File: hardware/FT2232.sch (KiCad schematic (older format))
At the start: 3 parts, among them U1 FT2232D

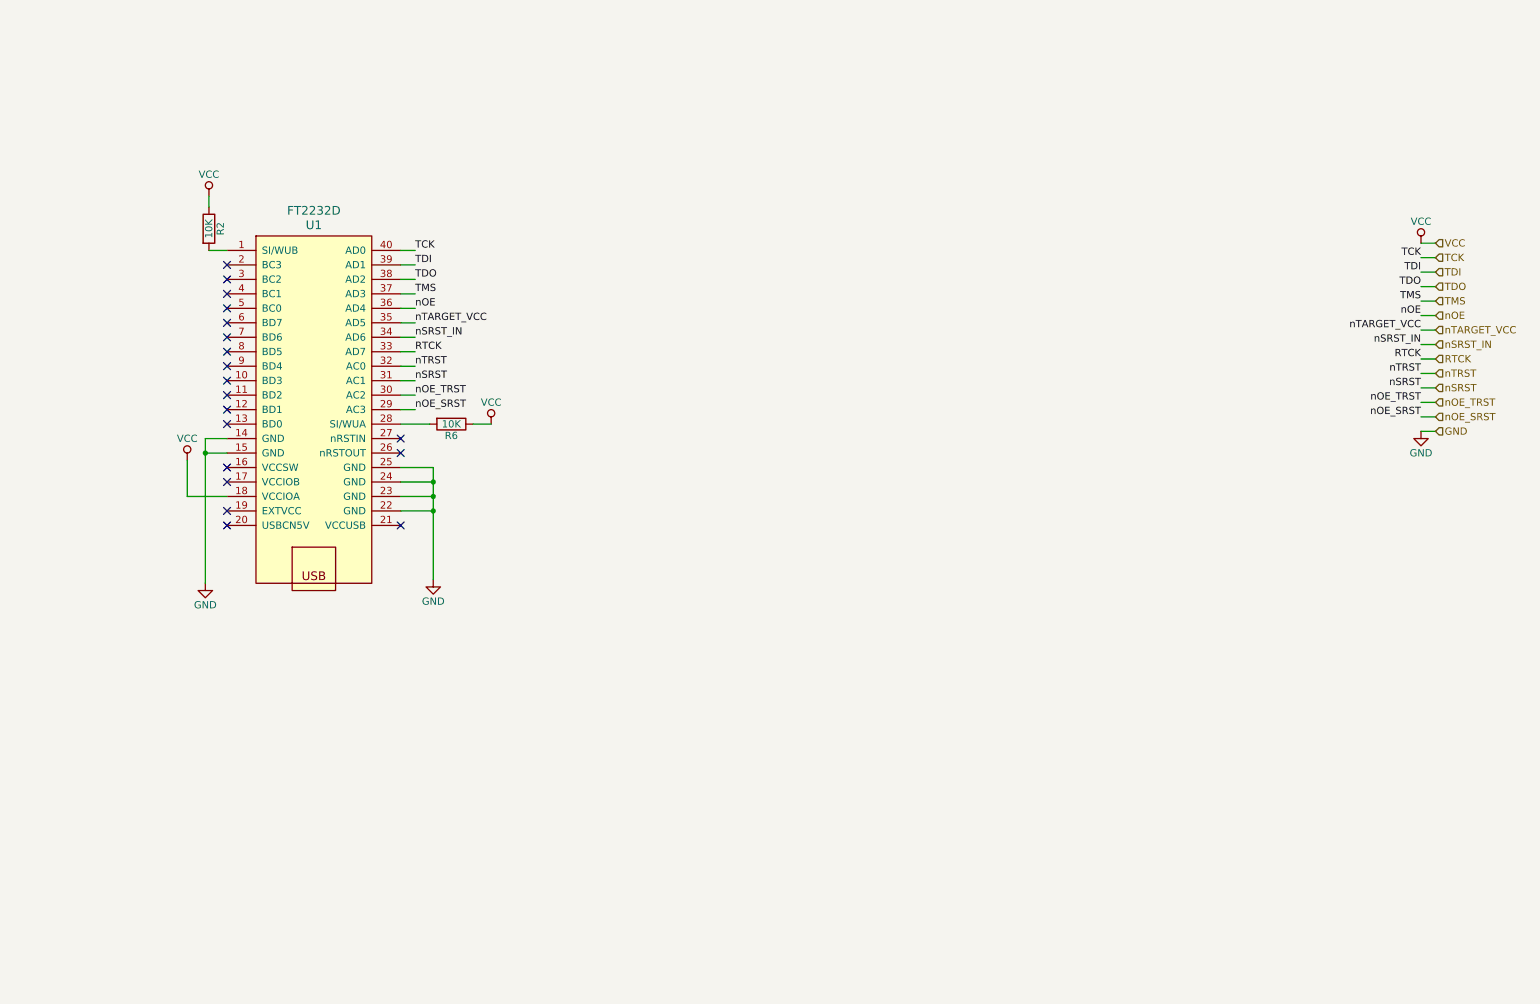
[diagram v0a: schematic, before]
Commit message: [WIP] hardware: Add FT2232D
It will replace AE_FT2232D in the near future.
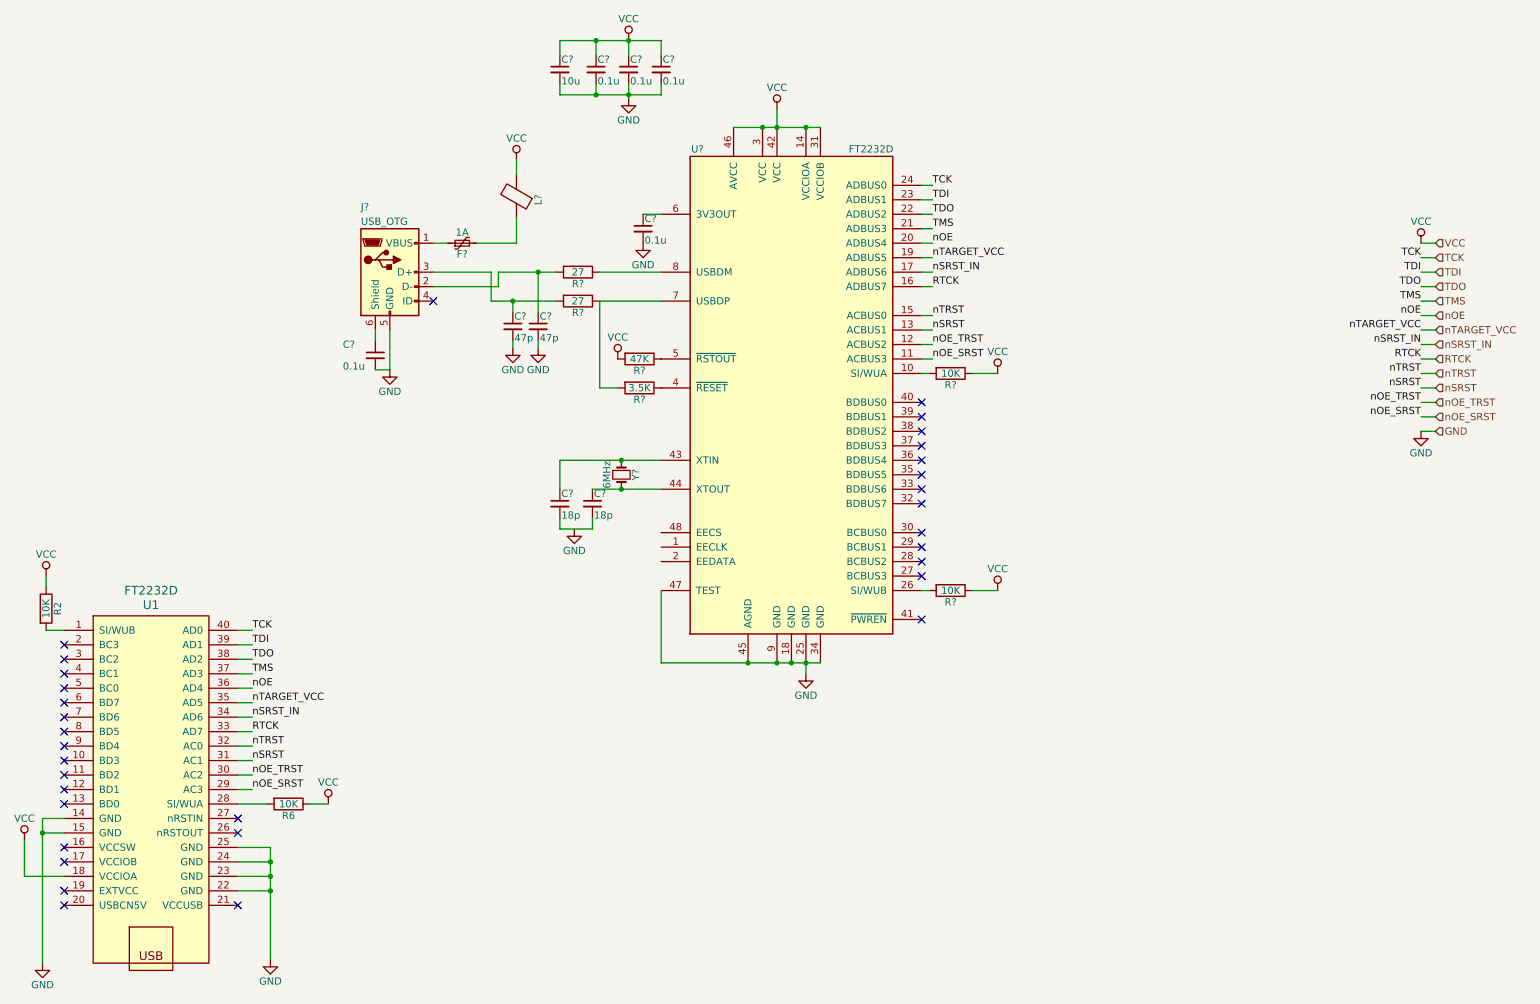
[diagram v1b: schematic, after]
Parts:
- added C? (x5): 0.1u, symbol C_Small
- added C? (x2): 47p, symbol C_Small
- added C? (x2): 18p, symbol C_Small
- added C?: 10u, symbol C_Small
- added F?: 1A, symbol Polyfuse_Small
- added J?: USB_OTG, symbol USB_OTG
- added L?: Ferrite_Bead, symbol Ferrite_Bead
- added R? (x2): 10K, Resistors_SMD:R_0805_HandSoldering, symbol R
- added R?: 47K, Resistors_SMD:R_0805_HandSoldering, symbol R
- added R?: 3.5K, Resistors_SMD:R_0805_HandSoldering, symbol R
- added R? (x2): 27, Resistors_SMD:R_0805_HandSoldering, symbol R
- added U?: FT2232D, Package_QFP:LQFP-48_7x7mm_P0.5mm, symbol FT2232D
- added Y?: 6MHz, symbol Crystal_Small
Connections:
- net GND: now also C?.2, C?.2, C?.2, C?.2, C?.2, C?.2, C?.2, C?.2, J?.5 (GND), U?.18 (GND), U?.25 (GND), U?.34 (GND), U?.45 (AGND), U?.47 (TEST), U?.9 (GND)
- net RTCK: now also U?.16 (ADBUS7)
- net TCK: now also U?.24 (ADBUS0)
- net TDI: now also U?.23 (ADBUS1)
- net TDO: now also U?.22 (ADBUS2)
- net TMS: now also U?.21 (ADBUS3)
- net VCC: now also C?.1, C?.1, C?.1, C?.1, L?.2, R?.1, R?.1, R?.2, U?.14 (VCCIOA), U?.3 (VCC), U?.31 (VCCIOB), U?.42 (VCC), U?.46 (AVCC)
- net nOE: now also U?.20 (ADBUS4)
- net nOE_SRST: now also U?.11 (ACBUS3)
- net nOE_TRST: now also U?.12 (ACBUS2)
- net nSRST: now also U?.13 (ACBUS1)
- net nSRST_IN: now also U?.17 (ADBUS6)
- net nTARGET_VCC: now also U?.19 (ADBUS5)
- net nTRST: now also U?.15 (ACBUS0)
- new net: R?.2, U?.10 (SI/WUA)
- new net: R?.2, U?.26 (SI/WUB)
- new net: R?.1, U?.4 (~RESET)
- new net: C?.1, U?.43 (XTIN), Y?.1
- new net: C?.1, U?.44 (XTOUT), Y?.2
- new net: R?.1, U?.5 (~RSTOUT)
- new net: C?.1, U?.6 (3V3OUT)
- new net: R?.1, R?.2, U?.7 (USBDP)
- new net: R?.1, U?.8 (USBDM)
- new net: C?.1, J?.3 (D+), R?.2
- new net: C?.1, J?.2 (D-), R?.2
- new net: F?.1, J?.1 (VBUS)
- new net: C?.1, J?.6 (Shield)
- new net: C?.2, C?.2
- new net: F?.2, L?.1
- no-connect marks 19 -> 33
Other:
- moved on the sheet: R2, R6, U1
